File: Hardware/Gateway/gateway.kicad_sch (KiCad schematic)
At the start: 0 parts

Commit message: Added untested op amp circuits for all three devices.
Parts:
- added C1, C2: 4.7uF?, 16V, symbol Device:C_Small
- added J1 (x2), J3 (x2): Esp32 socket, Connector_PinSocket_2.54mm:PinSocket_1x19_P2.54mm_Vertical, symbol Connector:Conn_01x19_Socket
- added J7: AudioJack2_Ground, symbol Connector_Audio:AudioJack2_Ground
- added R1: 500k?, symbol Device:R_Small
- added R3, R4, R5, R6: 100k, symbol Device:R_Small
- added RV1: 1M?, symbol Device:R_Potentiometer_Trim
- added U1: LM324, symbol Amplifier_Operational:LM324
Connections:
- new net: C1.2, R1.1, R5.1, R6.2
- new net: C2.2, J7.S, J7.T
- new net: C2.1, RV1.1, RV1.2, U1.1
- new net: R1.2, RV1.3, U1.2 (-)
- new net: R3.2, R4.1, U1.3 (+)
- new net +3.3V: J3.1 (Pin_1), J3.1 (Pin_1), R4.2, R5.2
- new net +5V: J3.19 (Pin_19), J3.19 (Pin_19), U1.4 (V+)
- new net 0: J1.14 (Pin_14), J1.14 (Pin_14)
- new net 12: J3.13 (Pin_13), J3.13 (Pin_13)
- new net 13: J3.15 (Pin_15), J3.15 (Pin_15)
- new net 14: J3.12 (Pin_12), J3.12 (Pin_12)
- new net 15: J1.16 (Pin_16), J1.16 (Pin_16)
- new net 16: J1.12 (Pin_12), J1.12 (Pin_12)
- new net 17: J1.11 (Pin_11), J1.11 (Pin_11)
- new net 18: J1.9 (Pin_9), J1.9 (Pin_9)
- new net 19: J1.8 (Pin_8), J1.8 (Pin_8)
- new net 2: J1.15 (Pin_15), J1.15 (Pin_15)
- new net 21: J1.6 (Pin_6), J1.6 (Pin_6)
- new net 22: J1.3 (Pin_3), J1.3 (Pin_3)
- new net 23: J1.2 (Pin_2), J1.2 (Pin_2)
- new net 26: J3.10 (Pin_10), J3.10 (Pin_10)
- new net 27: J3.11 (Pin_11), J3.11 (Pin_11)
- new net 32: J3.7 (Pin_7), J3.7 (Pin_7)
- new net 33: J3.8 (Pin_8), J3.8 (Pin_8)
- new net 34: J3.5 (Pin_5), J3.5 (Pin_5)
- new net 35: J3.6 (Pin_6), J3.6 (Pin_6)
- new net 4: J1.13 (Pin_13), J1.13 (Pin_13)
- new net 5: J1.10 (Pin_10), J1.10 (Pin_10)
- new net CLK: J1.19 (Pin_19), J1.19 (Pin_19)
- new net CMD: J3.18 (Pin_18), J3.18 (Pin_18)
- new net D1: J1.17 (Pin_17), J1.17 (Pin_17)
- new net D2: J3.16 (Pin_16), J3.16 (Pin_16)
- new net D3: J3.17 (Pin_17), J3.17 (Pin_17)
- new net D9: J1.18 (Pin_18), J1.18 (Pin_18)
- new net DAC1: C1.1, J3.9 (Pin_9), J3.9 (Pin_9)
- new net EN: J3.2 (Pin_2), J3.2 (Pin_2)
- new net GND: J1.1 (Pin_1), J1.1 (Pin_1), J1.7 (Pin_7), J1.7 (Pin_7), J3.14 (Pin_14), J3.14 (Pin_14), J7.G, R3.1, R6.1, U1.11 (V-)
- new net RX: J1.5 (Pin_5), J1.5 (Pin_5)
- new net TX: J1.4 (Pin_4), J1.4 (Pin_4)
- new net VN: J3.4 (Pin_4), J3.4 (Pin_4)
- new net VP: J3.3 (Pin_3), J3.3 (Pin_3)
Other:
- note added: "ESP32"
- note added: "LM324 can output from 0v to VCC-1.5, so 0-3.5v"
- note added: "Separate 5v ldo?"

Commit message: added PDF of hardware. Very small (if any) hardware changes.
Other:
- note added: "SPI or serial communication"
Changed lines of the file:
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@@
+    (effects (font (size 1.27 1.27)) (justify left bottom))
+  )
+  (text "SPI or serial communication" (at 95.25 67.31 0)
     (effects (font (size 1.27 1.27)) (justify left bottom))
   )

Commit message: Greatly simplified the gateway/speaker module. Added a rectifying circuit and a comparator circuit to the bass drum module. Solidified some component values. Added decoupling capacitors to the schematic.
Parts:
- removed C2: 4.7uF?, 16V, symbol Device:C_Small
- removed R3, R4, R5, R6: 100k, symbol Device:R_Small
- removed RV1: 1M?, symbol Device:R_Potentiometer_Trim
- removed U1: LM324, symbol Amplifier_Operational:LM324
- added RV1: 10k, symbol Device:R_Potentiometer
- R1: value 500k? -> 10k
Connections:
- net GND: now also RV1.3
- net at J7.S, J7.T: now also RV1.2
- net at R1.2: now also RV1.1
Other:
- note added: "Assume high-Z input on external speaker."
- note removed: "LM324 can output from 0v to VCC-1.5, so 0-3.5v"
- note removed: "Separate 5v ldo?"
- moved on the sheet: C1, J7

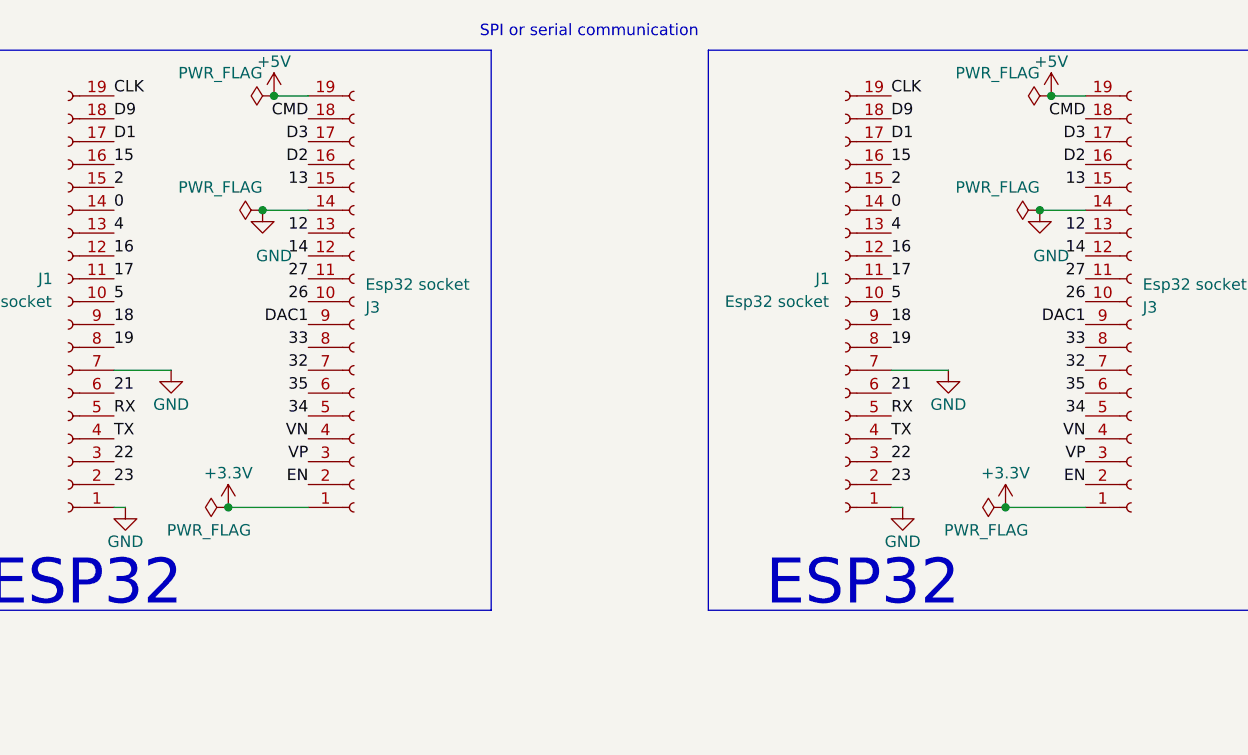
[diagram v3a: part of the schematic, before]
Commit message: added batteries to the schematic.
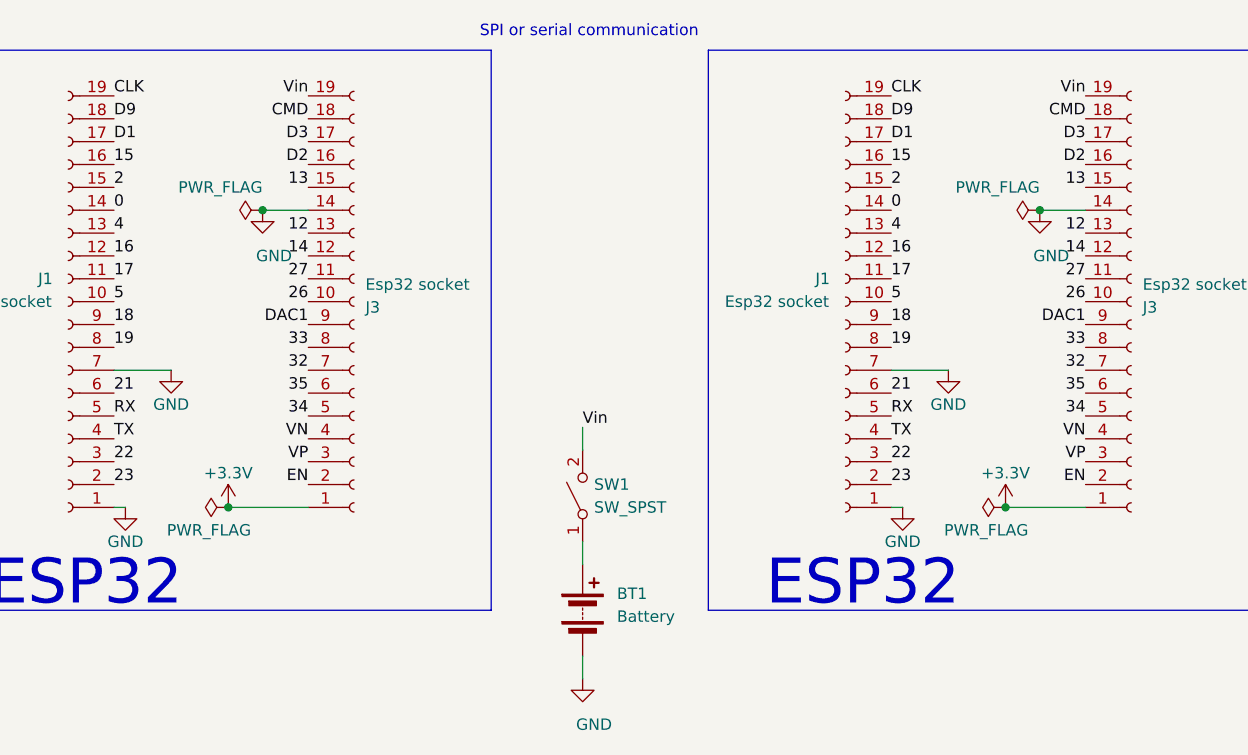
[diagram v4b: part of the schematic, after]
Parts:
- added BT1: Battery, symbol Device:Battery
- added SW1: SW_SPST, symbol Switch:SW_SPST
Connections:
- net GND: now also BT1.2 (-)
- net +5V renamed Vin
- net Vin: now also SW1.2 (B)
- new net: BT1.1 (+), SW1.1 (A)
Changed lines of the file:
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@@
   (junction (at 71.12 86.36) (diameter 0) (color 0 0 0 0)
   )
-  (junction (at 158.75 73.66) (diameter 0) (color 0 0 0 0)
-  )
   (junction (at 157.48 86.36) (diameter 0) (color 0 0 0 0)
   )
-  (junction (at 72.39 73.66) (diameter 0) (color 0 0 0 0)
-  )
   (wire (pts (xy 67.31 119.38) (xy 76.2 119.38))
     (stroke (width 0) (type default))
   )
+  (wire (pts (xy 106.68 110.49) (xy 106.68 113.03))
+    (stroke (width 0) (type default))
+  )
+  (wire (pts (xy 106.68 138.43) (xy 106.68 135.89))
+    (stroke (width 0) (type default))
+  )
   (wire (pts (xy 153.67 119.38) (xy 162.56 119.38))
     (stroke (width 0) (type default))
@@
     (stroke (width 0) (type default))
   )
-  (wire (pts (xy 158.75 73.66) (xy 162.56 73.66))
-    (stroke (width 0) (type default))
-  )
   (wire (pts (xy 140.97 104.14) (xy 147.32 104.14))
     (stroke (width 0) (type default))
   )
-  (wire (pts (xy 72.39 73.66) (xy 76.2 73.66))
-    (stroke (width 0) (type default))
-  )
   (wire (pts (xy 209.55 116.84) (xy 209.55 114.3))
+    (stroke (width 0) (type default))
+  )
+  (wire (pts (xy 106.68 123.19) (xy 106.68 125.73))
     (stroke (width 0) (type default))
   )
@@
     (effects (font (size 1.27 1.27)) (justify left bottom))
   )
+  (label "Vin" (at 76.2 73.66 180) (fields_autoplaced)
+    (effects (font (size 1.27 1.27)) (justify right bottom))
+  )
   (label "D3" (at 76.2 78.74 180) (fields_autoplaced)
     (effects (font (size 1.27 1.27)) (justify right bottom))
@@
     (effects (font (size 1.27 1.27)) (justify right bottom))
   )
+  (label "Vin" (at 106.68 110.49 0) (fields_autoplaced)
+    (effects (font (size 1.27 1.27)) (justify left bottom))
+  )
   (label "D9" (at 54.61 76.2 0) (fields_autoplaced)
     (effects (font (size 1.27 1.27)) (justify left bottom))
@@
   (label "5" (at 140.97 96.52 0) (fields_autoplaced)
     (effects (font (size 1.27 1.27)) (justify left bottom))
+  )
+  (label "Vin" (at 162.56 73.66 180) (fields_autoplaced)
+    (effects (font (size 1.27 1.27)) (justify right bottom))
   )
   (label "19" (at 54.61 101.6 0) (fields_autoplaced)
@@
     )
   )
-  (symbol (lib_id "power:+5V") (at 158.75 73.66 0) (unit 1)
-    (in_bom yes) (on_board yes) (dnp no) (fields_autoplaced)
-    (property "Reference" "#PWR01" (at 158.75 77.47 0)
-      (effects (font (size 1.27 1.27)) hide)
-    )
-    (property "Value" "+5V" (at 158.75 69.85 0)
-      (effects (font (size 1.27 1.27)))
-    )
-    (property "Footprint" "" (at 158.75 73.66 0)
-      (effects (font (size 1.27 1.27)) hide)
-    )
-    (property "Datasheet" "" (at 158.75 73.66 0)
-      (effects (font (size 1.27 1.27)) hide)
-    )
-    (pin "1")
-    (instances
-      (project "Aktuator-ESP"
-        (path "/355dd754-d0d4-46b9-8352-e30cc265914f"
-          (reference "#PWR01") (unit 1)
-        )
-      )
-      (project "Stink-overview"
-        (path "/cabf8207-5290-464d-a5db-d31c713ce03c/9cff79f6-1e38-4fd8-974e-e06f4e0c362c"
-          (reference "#PWR05") (unit 1)
-        )
-        (path "/cabf8207-5290-464d-a5db-d31c713ce03c/8d7bbeab-1973-44b8-aed2-4e4d1a62bc12"
-          (reference "#PWR015") (unit 1)
-        )
-      )
-    )
-  )
-  (symbol (lib_id "power:+5V") (at 72.39 73.66 0) (unit 1)
-    (in_bom yes) (on_board yes) (dnp no) (fields_autoplaced)
-    (property "Reference" "#PWR01" (at 72.39 77.47 0)
-      (effects (font (size 1.27 1.27)) hide)
-    )
-    (property "Value" "+5V" (at 72.39 69.85 0)
-      (effects (font (size 1.27 1.27)))
-    )
-    (property "Footprint" "" (at 72.39 73.66 0)
-      (effects (font (size 1.27 1.27)) hide)
-    )
-    (property "Datasheet" "" (at 72.39 73.66 0)
-      (effects (font (size 1.27 1.27)) hide)
-    )
-    (pin "1")
-    (instances
-      (project "Aktuator-ESP"
-        (path "/355dd754-d0d4-46b9-8352-e30cc265914f"
-          (reference "#PWR01") (unit 1)
-        )
-      )
-      (project "Stink-overview"
-        (path "/cabf8207-5290-464d-a5db-d31c713ce03c/9cff79f6-1e38-4fd8-974e-e06f4e0c362c"
-          (reference "#PWR05") (unit 1)
-        )
-        (path "/cabf8207-5290-464d-a5db-d31c713ce03c/8d7bbeab-1973-44b8-aed2-4e4d1a62bc12"
-          (reference "#PWR026") (unit 1)
-        )
-      )
-    )
-  )
   (symbol (lib_id "power:PWR_FLAG") (at 153.67 119.38 90) (unit 1)
     (in_bom yes) (on_board yes) (dnp no)
@@
     )
   )
+  (symbol (lib_id "Device:Battery") (at 106.68 130.81 0) (unit 1)
+    (in_bom yes) (on_board yes) (dnp no) (fields_autoplaced)
+    (property "Reference" "BT1" (at 110.49 128.9685 0)
+      (effects (font (size 1.27 1.27)) (justify left))
+    )
+    (property "Value" "Battery" (at 110.49 131.5085 0)
+      (effects (font (size 1.27 1.27)) (justify left))
+    )
+    (property "Footprint" "" (at 106.68 129.286 90)
+      (effects (font (size 1.27 1.27)) hide)
+    )
+    (property "Datasheet" "~" (at 106.68 129.286 90)
+      (effects (font (size 1.27 1.27)) hide)
+    )
+    (pin "1")
+    (pin "2")
+    (instances
+      (project "Stink-overview"
+        (path "/cabf8207-5290-464d-a5db-d31c713ce03c/c3cf50cb-25cf-454a-ad63-d86ff0651171"
+          (reference "BT1") (unit 1)
+        )
+        (path "/cabf8207-5290-464d-a5db-d31c713ce03c/8d7bbeab-1973-44b8-aed2-4e4d1a62bc12"
+          (reference "BT3") (unit 1)
+        )
+      )
+    )
+  )
   (symbol (lib_id "power:GND") (at 226.06 120.65 0) (mirror y) (unit 1)
     (in_bom yes) (on_board yes) (dnp no)
@@
     )
   )
+  (symbol (lib_id "Switch:SW_SPST") (at 106.68 118.11 90) (unit 1)
+    (in_bom yes) (on_board yes) (dnp no) (fields_autoplaced)
+    (property "Reference" "SW1" (at 107.95 116.84 90)
+      (effects (font (size 1.27 1.27)) (justify right))
+    )
+    (property "Value" "SW_SPST" (at 107.95 119.38 90)
+      (effects (font (size 1.27 1.27)) (justify right))
+    )
+    (property "Footprint" "" (at 106.68 118.11 0)
+      (effects (font (size 1.27 1.27)) hide)
+    )
+    (property "Datasheet" "~" (at 106.68 118.11 0)
+      (effects (font (size 1.27 1.27)) hide)
+    )
+    (pin "1")
+    (pin "2")
+    (instances
+      (project "Stink-overview"
+        (path "/cabf8207-5290-464d-a5db-d31c713ce03c/c3cf50cb-25cf-454a-ad63-d86ff0651171"
+          (reference "SW1") (unit 1)
+        )
+        (path "/cabf8207-5290-464d-a5db-d31c713ce03c/8d7bbeab-1973-44b8-aed2-4e4d1a62bc12"
+          (reference "SW3") (unit 1)
+        )
+      )
+    )
+  )
   (symbol (lib_id "power:GND") (at 55.88 119.38 0) (mirror y) (unit 1)
     (in_bom yes) (on_board yes) (dnp no)
@@
     )
   )
-  (symbol (lib_id "power:PWR_FLAG") (at 72.39 73.66 90) (unit 1)
-    (in_bom yes) (on_board yes) (dnp no)
-    (property "Reference" "#FLG02" (at 70.485 73.66 0)
-      (effects (font (size 1.27 1.27)) hide)
-    )
-    (property "Value" "PWR_FLAG" (at 71.12 71.12 90)
-      (effects (font (size 1.27 1.27)) (justify left))
-    )
-    (property "Footprint" "" (at 72.39 73.66 0)
-      (effects (font (size 1.27 1.27)) hide)
-    )
-    (property "Datasheet" "~" (at 72.39 73.66 0)
-      (effects (font (size 1.27 1.27)) hide)
-    )
-    (pin "1")
-    (instances
-      (project "Aktuator-ESP"
-        (path "/355dd754-d0d4-46b9-8352-e30cc265914f"
-          (reference "#FLG02") (unit 1)
-        )
-      )
-      (project "Stink-overview"
-        (path "/cabf8207-5290-464d-a5db-d31c713ce03c/9cff79f6-1e38-4fd8-974e-e06f4e0c362c"
-          (reference "#FLG03") (unit 1)
-        )
-        (path "/cabf8207-5290-464d-a5db-d31c713ce03c/8d7bbeab-1973-44b8-aed2-4e4d1a62bc12"
-          (reference "#FLG012") (unit 1)
-        )
-      )
-    )
-  )
-  (symbol (lib_id "power:PWR_FLAG") (at 158.75 73.66 90) (unit 1)
-    (in_bom yes) (on_board yes) (dnp no)
-    (property "Reference" "#FLG02" (at 156.845 73.66 0)
-      (effects (font (size 1.27 1.27)) hide)
-    )
-    (property "Value" "PWR_FLAG" (at 157.48 71.12 90)
-      (effects (font (size 1.27 1.27)) (justify left))
-    )
-    (property "Footprint" "" (at 158.75 73.66 0)
-      (effects (font (size 1.27 1.27)) hide)
-    )
-    (property "Datasheet" "~" (at 158.75 73.66 0)
-      (effects (font (size 1.27 1.27)) hide)
-    )
-    (pin "1")
-    (instances
-      (project "Aktuator-ESP"
-        (path "/355dd754-d0d4-46b9-8352-e30cc265914f"
-          (reference "#FLG02") (unit 1)
-        )
-      )
-      (project "Stink-overview"
-        (path "/cabf8207-5290-464d-a5db-d31c713ce03c/9cff79f6-1e38-4fd8-974e-e06f4e0c362c"
-          (reference "#FLG03") (unit 1)
-        )
-        (path "/cabf8207-5290-464d-a5db-d31c713ce03c/8d7bbeab-1973-44b8-aed2-4e4d1a62bc12"
-          (reference "#FLG09") (unit 1)
-        )
-      )
+  (symbol (lib_id "power:GND") (at 106.68 138.43 0) (unit 1)
+    (in_bom yes) (on_board yes) (dnp no)
+    (property "Reference" "#PWR02" (at 106.68 144.78 0)
+      (effects (font (size 1.27 1.27)) hide)
+    )
+    (property "Value" "GND" (at 107.95 143.51 0)
+      (effects (font (size 1.27 1.27)))
+    )
+    (property "Footprint" "" (at 106.68 138.43 0)
+      (effects (font (size 1.27 1.27)) hide)
+    )
+    (property "Datasheet" "" (at 106.68 138.43 0)
+      (effects (font (size 1.27 1.27)) hide)
+    )
+    (pin "1")
+    (instances
+      (project "Aktuator-ESP"
+        (path "/355dd754-d0d4-46b9-8352-e30cc265914f"
+          (reference "#PWR02") (unit 1)
+        )
+      )
+      (project "Stink-overview"
+        (path "/cabf8207-5290-464d-a5db-d31c713ce03c/9cff79f6-1e38-4fd8-974e-e06f4e0c362c"
+          (reference "#PWR031") (unit 1)
+        )
+        (path "/cabf8207-5290-464d-a5db-d31c713ce03c/8d7bbeab-1973-44b8-aed2-4e4d1a62bc12"
+          (reference "#PWR041") (unit 1)
+        )
+        (path "/cabf8207-5290-464d-a5db-d31c713ce03c/c3cf50cb-25cf-454a-ad63-d86ff0651171"
+          (reference "#PWR035") (unit 1)
+        )
+      )

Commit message: Updated PDF.
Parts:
- R1: value 10k -> 20k
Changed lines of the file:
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@@
       (effects (font (size 1.27 1.27)) (justify left))
     )
-    (property "Value" "10k" (at 212.09 102.87 0)
+    (property "Value" "20k" (at 212.09 102.87 0)
       (effects (font (size 1.27 1.27)) (justify left))
     )
